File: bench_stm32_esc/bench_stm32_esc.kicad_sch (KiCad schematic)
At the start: 107 parts, among them CN1 S6B-PH-K-S-, CN10 Conn_02x19_Odd_Even, CN7 Conn_02x19_Odd_Even, J1 XT60PW-M, Q1 CSD19532Q5B, Q2 CSD19532Q5B, Q3 CSD19532Q5B, Q4 CSD19532Q5B, Q5 CSD19532Q5B, Q6 CSD19532Q5B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

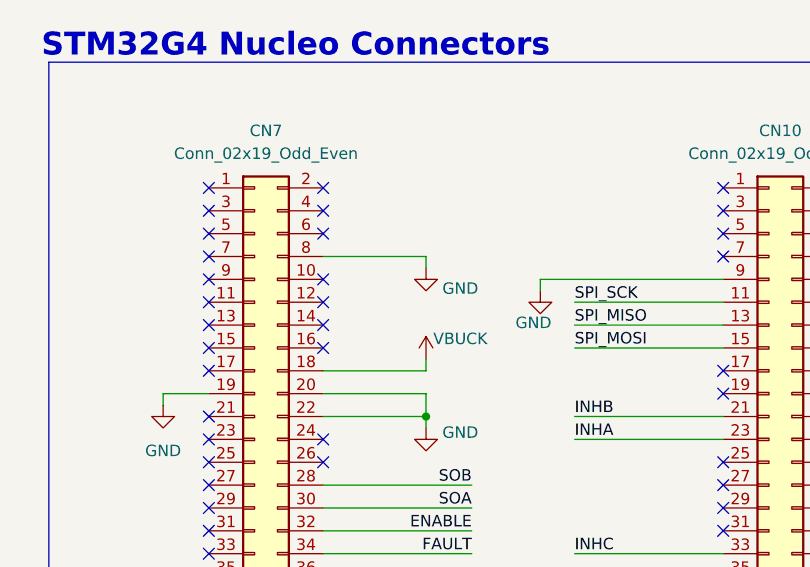
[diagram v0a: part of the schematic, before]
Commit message: Fixed 5V input to NUCLEO Board
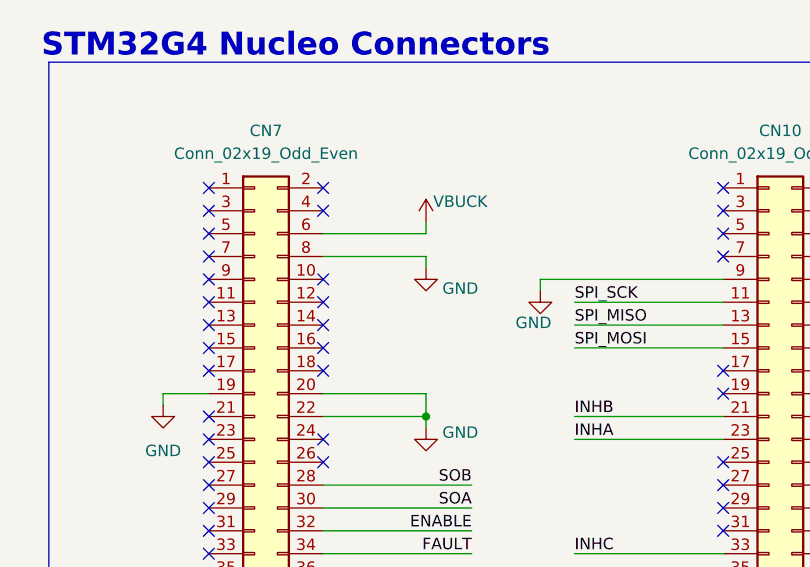
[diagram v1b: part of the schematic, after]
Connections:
- net VBUCK: now also CN7.6 (Pin_6); no longer CN7.18 (Pin_18)
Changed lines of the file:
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@@
 	)
 	(no_connect
-		(at 53.34 40.64)
-	)
-	(no_connect
 		(at 40.64 68.58)
 	)
@@
 	)
 	(no_connect
+		(at 53.34 55.88)
+	)
+	(no_connect
 		(at 53.34 45.72)
 	)
@@
 	(wire
 		(pts
-			(xy 64.77 54.61) (xy 64.77 55.88)
-		)
-		(stroke
-			(width 0)
-			(type default)
-		)
-	)
-	(wire
-		(pts
 			(xy 154.94 176.53) (xy 157.48 176.53)
 		)
@@
 	(wire
 		(pts
-			(xy 53.34 55.88) (xy 64.77 55.88)
+			(xy 359.41 59.69) (xy 359.41 64.77)
 		)
 		(stroke
@@
 	(wire
 		(pts
-			(xy 359.41 59.69) (xy 359.41 64.77)
+			(xy 255.27 176.53) (xy 255.27 179.07)
 		)
 		(stroke
@@
 	(wire
 		(pts
-			(xy 255.27 176.53) (xy 255.27 179.07)
+			(xy 269.24 72.39) (xy 279.4 72.39)
 		)
 		(stroke
@@
 	(wire
 		(pts
-			(xy 269.24 72.39) (xy 279.4 72.39)
+			(xy 40.64 113.03) (xy 49.53 113.03)
 		)
 		(stroke
@@
 	(wire
 		(pts
-			(xy 40.64 113.03) (xy 49.53 113.03)
+			(xy 142.24 252.73) (xy 142.24 257.81)
 		)
 		(stroke
@@
 	(wire
 		(pts
-			(xy 142.24 252.73) (xy 142.24 257.81)
+			(xy 210.82 110.49) (xy 222.25 110.49)
 		)
 		(stroke
@@
 	(wire
 		(pts
-			(xy 210.82 110.49) (xy 222.25 110.49)
+			(xy 64.77 39.37) (xy 64.77 40.64)
 		)
 		(stroke
@@
 	(wire
 		(pts
+			(xy 53.34 40.64) (xy 64.77 40.64)
+		)
+		(stroke
+			(width 0)
+			(type default)
+		)
+	)
+	(wire
+		(pts
 			(xy 157.48 176.53) (xy 175.26 176.53)
 		)
@@
 	)
 	(symbol
+		(lib_id "power:+3V3")
+		(at 64.77 39.37 0)
+		(unit 1)
+		(body_style 1)
+		(exclude_from_sim no)
+		(in_bom yes)
+		(on_board yes)
+		(in_pos_files yes)
+		(dnp no)
+		(property "Reference" "#PWR06"
+			(at 64.77 43.18 0)
+			(hide yes)
+			(show_name no)
+			(do_not_autoplace no)
+			(effects
+				(font
+					(size 1.27 1.27)
+				)
+			)
+		)
+		(property "Value" "VBUCK"
+			(at 68.58 37.084 0)
+			(show_name no)
+			(do_not_autoplace no)
+			(effects
+				(font
+					(size 1.27 1.27)
+				)
+			)
+		)
+		(property "Footprint" ""
+			(at 64.77 39.37 0)
+			(hide yes)
+			(show_name no)
+			(do_not_autoplace no)
+			(effects
+				(font
+					(size 1.27 1.27)
+				)
+			)
+		)
+		(property "Datasheet" ""
+			(at 64.77 39.37 0)
+			(hide yes)
+			(show_name no)
+			(do_not_autoplace no)
+			(effects
+				(font
+					(size 1.27 1.27)
+				)
+			)
+		)
+		(property "Description" "Power symbol creates a global label with name \"+3V3\""
+			(at 64.77 39.37 0)
+			(hide yes)
+			(show_name no)
+			(do_not_autoplace no)
+			(effects
+				(font
+					(size 1.27 1.27)
+				)
+			)
+		)
+		(pin "1"
+		)
+		(instances
+			(project "bench_stm32_esc"
+				(path "/746d987d-06f7-4596-a601-faf34de29dec"
+					(reference "#PWR06")
+					(unit 1)
+				)
+			)
+		)
+	)
+	(symbol
 		(lib_id "Device:R")
 		(at 59.69 220.98 0)
@@
 					(unit 1)
 				)
-			)
-		)
-	)
-	(symbol
-		(lib_id "power:+3V3")
-		(at 64.77 54.61 0)
-		(unit 1)
-		(body_style 1)
-		(exclude_from_sim no)
-		(in_bom yes)
-		(on_board yes)
-		(in_pos_files yes)
-		(dnp no)
-		(property "Reference" "#PWR06"
-			(at 64.77 58.42 0)
-			(hide yes)
-			(show_name no)
-			(do_not_autoplace no)
-			(effects
-				(font
-					(size 1.27 1.27)
-				)
-			)
-		)
-		(property "Value" "VBUCK"
-			(at 68.58 52.324 0)
-			(show_name no)
-			(do_not_autoplace no)
-			(effects
-				(font
-					(size 1.27 1.27)
-				)
-			)
-		)
-		(property "Footprint" ""
-			(at 64.77 54.61 0)
-			(hide yes)
-			(show_name no)
-			(do_not_autoplace no)
-			(effects
-				(font
-					(size 1.27 1.27)
-				)
-			)
-		)
-		(property "Datasheet" ""
-			(at 64.77 54.61 0)
-			(hide yes)
-			(show_name no)
-			(do_not_autoplace no)
-			(effects
-				(font
-					(size 1.27 1.27)
-				)
-			)
-		)
-		(property "Description" "Power symbol creates a global label with name \"+3V3\""
-			(at 64.77 54.61 0)
-			(hide yes)
-			(show_name no)
-			(do_not_autoplace no)
-			(effects
-				(font
-					(size 1.27 1.27)
-				)
-			)
-		)
-		(pin "1"
-		)
-		(instances
-			(project "bench_stm32_esc"
-				(path "/746d987d-06f7-4596-a601-faf34de29dec"
-					(reference "#PWR06")
-					(unit 1)
-				)
